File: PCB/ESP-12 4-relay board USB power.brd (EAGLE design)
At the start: 94 x 85 mm, 51 parts, among them J1 OUT1, J2 OUT2, J3 IN, J4 OUT3, J5 OUT4, K1 SRD-05VDC-SL-C, K2 SRD-05VDC-SL-C, K3 SRD-05VDC-SL-C, K4 SRD-05VDC-SL-C, Q1 2N7702P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

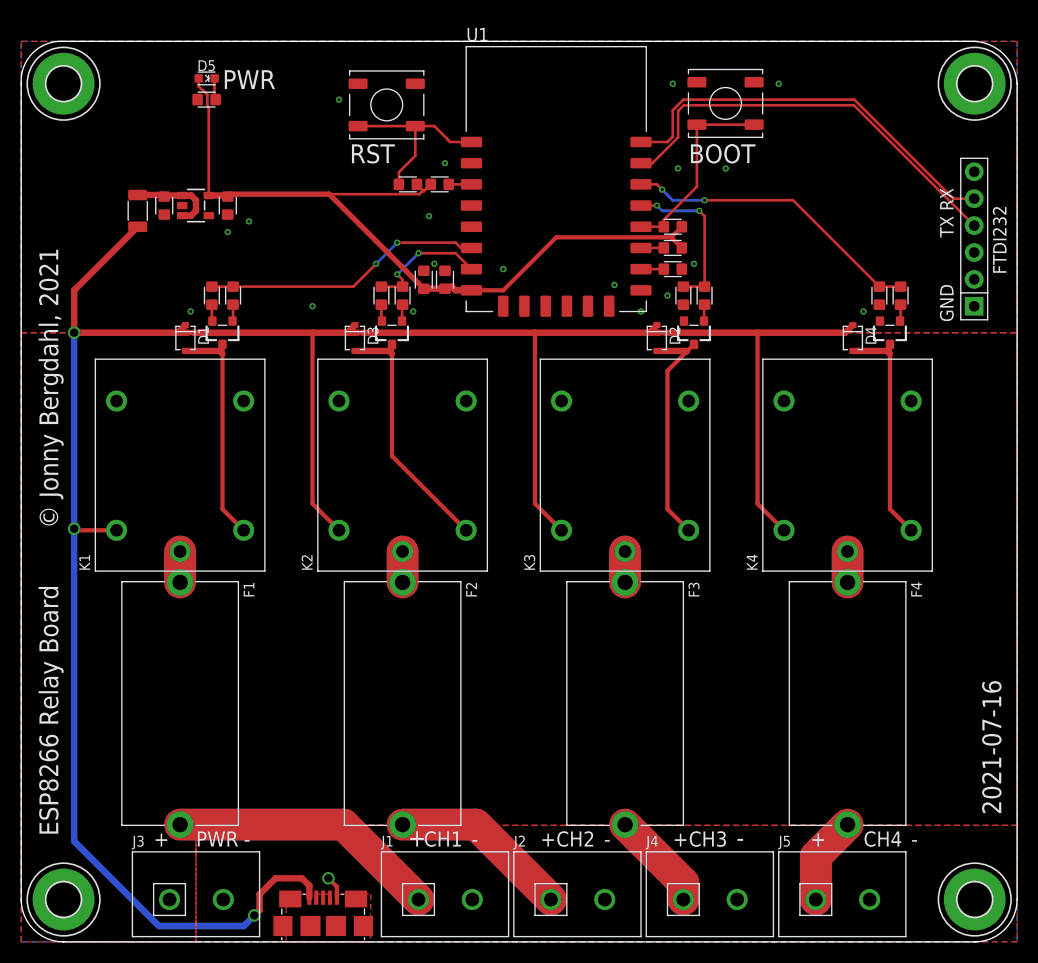
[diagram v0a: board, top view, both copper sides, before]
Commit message: Switch NC and NO on relays
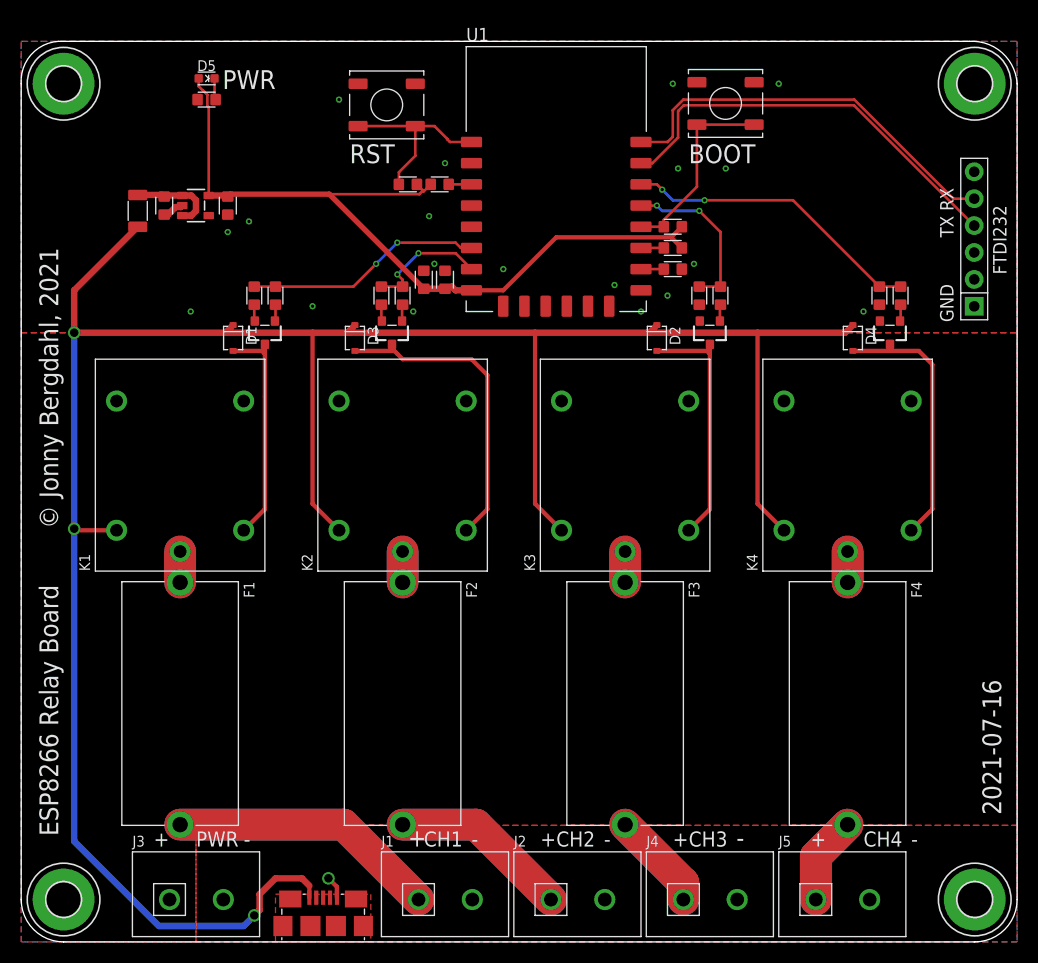
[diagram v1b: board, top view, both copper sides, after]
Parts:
- moved D1 4.50 mm to (20.0, 57.0)
- moved Q1 4.00 mm to (23.0, 57.5)
- moved R5 4.00 mm to (24.0, 61.0)
- moved R6 4.00 mm to (22.0, 61.0)
- moved Q3 1.50 mm to (65.0, 57.5)
- moved R10 1.50 mm to (64.0, 61.0)
- moved R9 1.50 mm to (66.0, 61.0)
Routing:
- net N$8: track 24.2 -> 29.7 mm
- net CH1: track 26.4 -> 22.4 mm
- net N$17: track 22.1 -> 25.1 mm
- net GND: track 5.30 -> 7.35 mm
- net N$12: track 22.2 -> 23.5 mm
- net VUSB: track 228.9 -> 230.0 mm
- net N$1: track 22.1 -> 21.5 mm
- net CH3: track 15.1 -> 15.7 mm
